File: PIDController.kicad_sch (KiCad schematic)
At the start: 27 parts, among them J1 Jack-DC, J2 Jack-DC, J3 Screw_Terminal_01x02, J4 Jack-DC, J5 Jack-DC, M1 Motor_DC, Q1 BD433, Q2 BD434, U1 LM324, U2 LM324

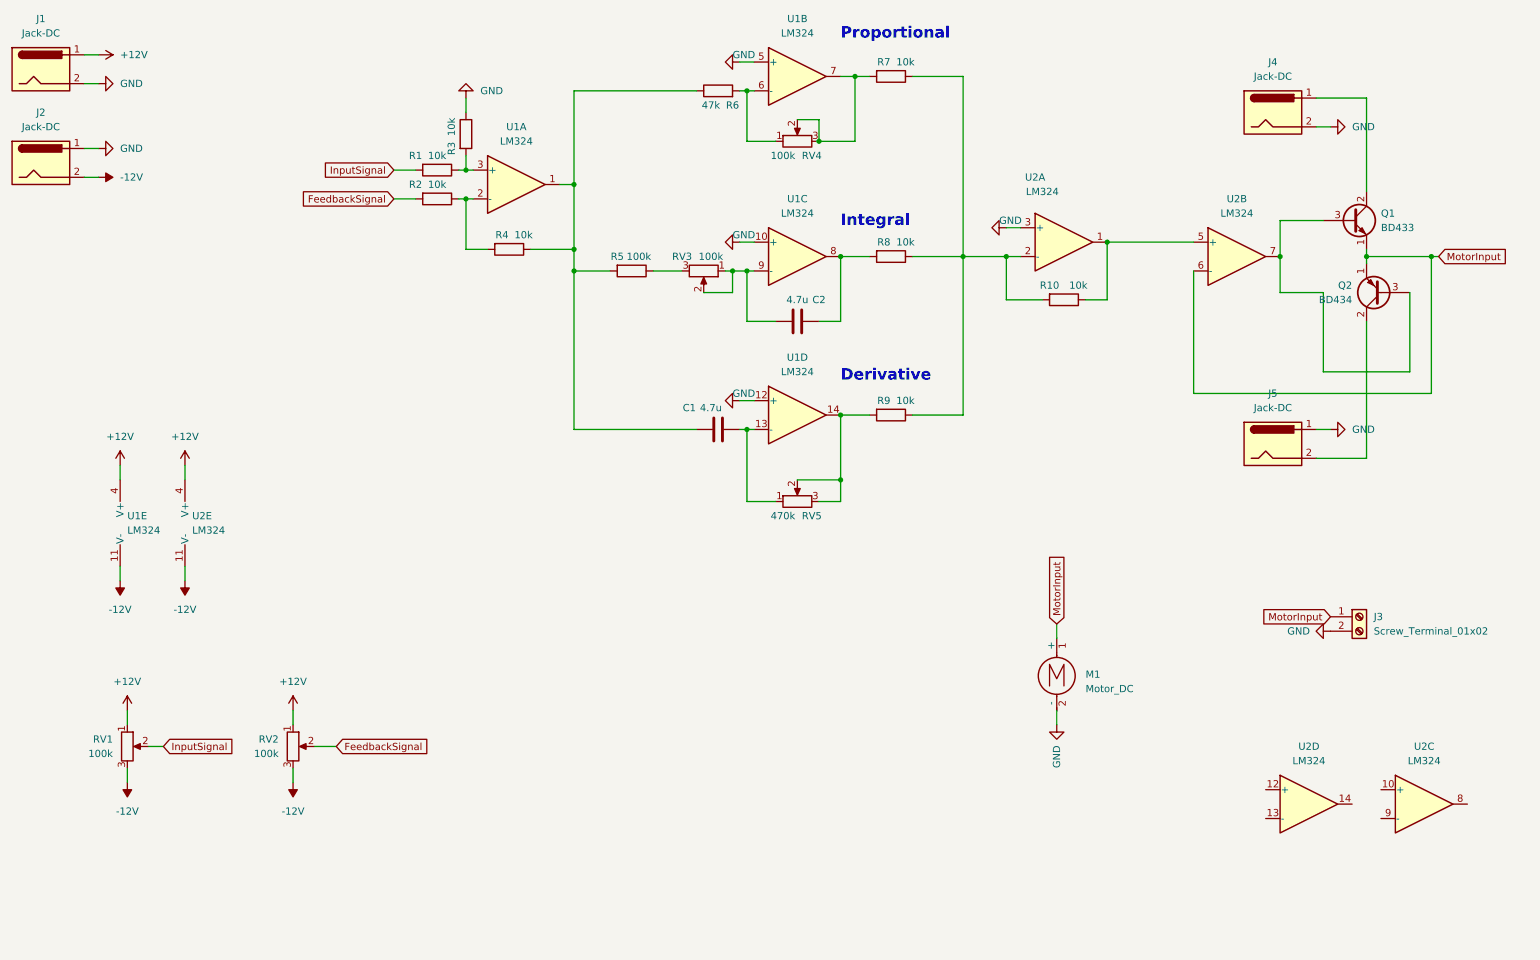
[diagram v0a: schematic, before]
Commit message: improved the general design, added ground plane, silkmask etc.
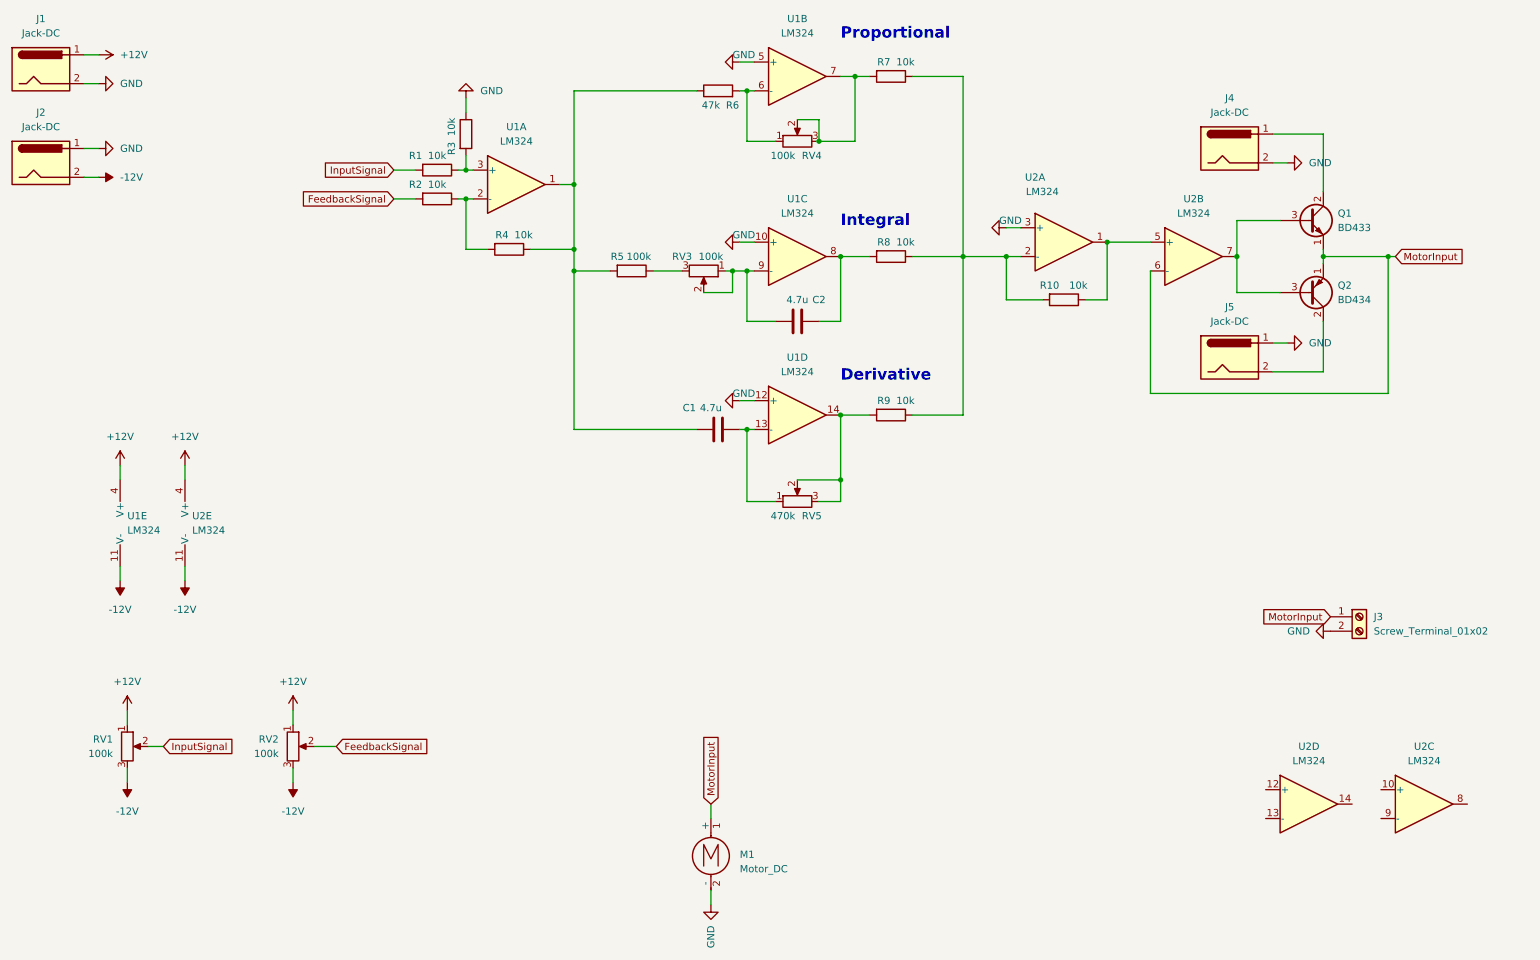
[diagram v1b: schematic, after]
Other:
- moved on the sheet: J4, J5, M1, Q1, Q2, U2B
